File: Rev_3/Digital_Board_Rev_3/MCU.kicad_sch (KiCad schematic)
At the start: 9 parts, among them U2 STM32G474VBTx

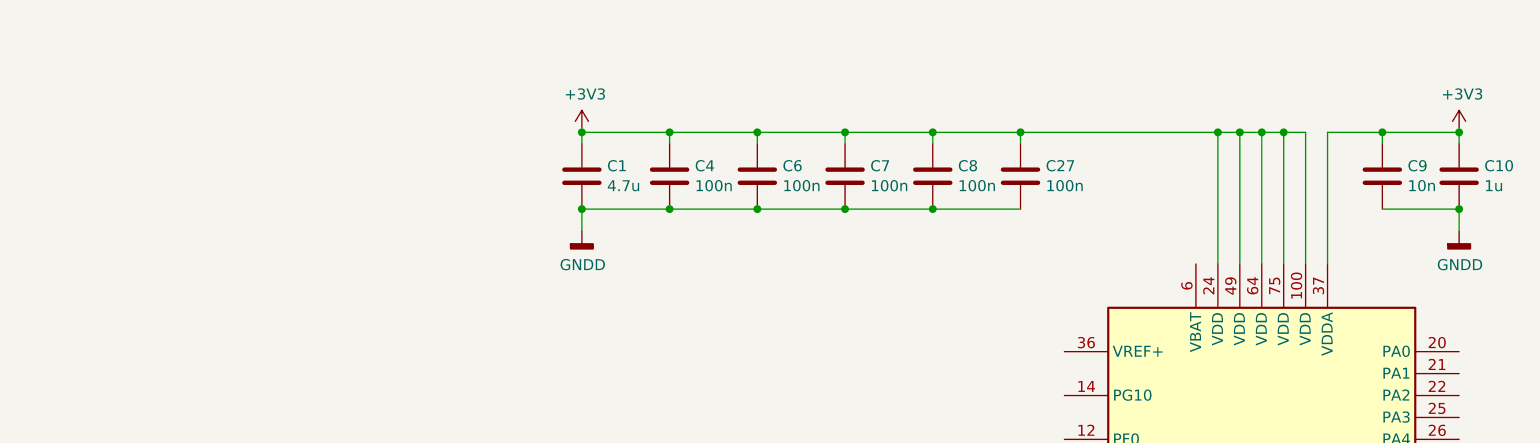
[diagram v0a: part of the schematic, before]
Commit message: Pivoting to Passive Jack Boards
Finalized layout for input/output Jack Boards, which are now completely passive and connected with board-to-board connectors. Schematics are not updated yet, just figuring out placement/dimensions.
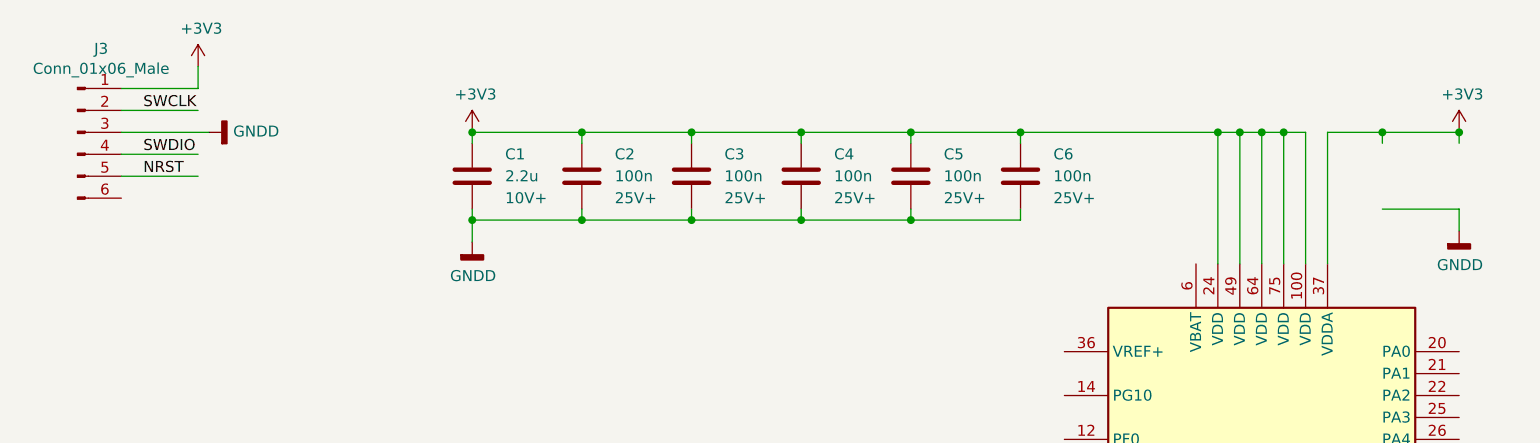
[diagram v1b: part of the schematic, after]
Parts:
- removed C1: 4.7u, Capacitor_SMD:C_0805_2012Metric_Pad1.18x1.45mm_HandSolder, symbol Device:C
- removed C10: 1u, Capacitor_SMD:C_0805_2012Metric_Pad1.18x1.45mm_HandSolder, symbol Device:C
- removed C27, C4, C6, C7, C8: 100n, Capacitor_SMD:C_0805_2012Metric_Pad1.18x1.45mm_HandSolder, symbol Device:C
- removed C9: 10n, Capacitor_SMD:C_0805_2012Metric_Pad1.18x1.45mm_HandSolder, symbol Device:C
- added C1: 2.2u, Capacitor_SMD:C_0603_1608Metric, symbol #gplm:cap/RES-4007-02U2
- added C2, C3, C4, C5, C6: 100n, Capacitor_SMD:C_0402_1005Metric, symbol #gplm:cap/RES-4003-100N
- added J3: Conn_01x06_Male, Connector_PinHeader_2.54mm:PinHeader_1x06_P2.54mm_Vertical, symbol Digital Board Rev 2-rescue:Conn_01x06_Male-Connector
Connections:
- net +3V3: now also C1.1, C2.1, C3.1, C4.1, C5.1, C6.1, J3.1 (Pin_1)
- net GNDD: now also C1.2, C2.2, C3.2, C4.2, C5.2, C6.2, J3.3 (Pin_3)
- new net NRST: J3.5 (Pin_5)
- new net SWCLK: J3.2 (Pin_2)
- new net SWDIO: J3.4 (Pin_4)
